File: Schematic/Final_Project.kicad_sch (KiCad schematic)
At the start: 82 parts, among them Q1 PMOS, U1 74HC595, U10 74HC595, U11 74HC595, U12 74HC595, U13 TLC59211IPWR, U14 TLC59211IPWR, U15 TLC59211IPWR, U16 TLC59211IPWR, U17 74HC595, U2 TLC59211IPWR, U3 74HC595, U4 TLC59211IPWR, U5 74HC595, U6 74HC595, U7 TLC59211IPWR, U8 TLC59211IPWR, U9 74HC595

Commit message: SemiFinal Schematic
unknown rgb layout for the Ebay LEDs
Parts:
- removed D1, D10, D11, D12, D13, D14, D15, D16, D17, D18, D19, D2, D20, D21, D22, D23, D24, D25, D26, D27, D28, D29, D3, D30, D31, D32, D33, D34, D35, D36, D37, D38, D39, D4, D40, D41, D42, D43, D44, D45, D46, D47, D48, D49, D5, D50, D51, D52, D53, D54, D55, D56, D57, D58, D59, D6, D60, D61, D62, D63, D64, D7, D8, D9: LED, symbol Device:LED
- removed U1, U10, U11, U12, U3, U5, U6, U9: 74HC595, symbol 74xx:74HC595
- removed U13, U14, U15, U16, U2, U4, U7, U8: TLC59211IPWR, PW20, symbol TLC59211:TLC59211IPWR
- added D1, D10, D11, D12, D13, D14, D15, D16, D17, D18, D19, D2, D20, D21, D22, D23, D24, D25, D26, D27, D28, D29, D3, D30, D31, D32, D33, D34, D35, D36, D37, D38, D39, D4, D40, D41, D42, D43, D44, D45, D46, D47, D48, D49, D5, D50, D51, D52, D53, D54, D55, D56, D57, D58, D59, D6, D60, D61, D62, D63, D64, D7, D8, D9: LED_ARBG, symbol Device:LED_ARBG
- added R_b1, R_b10, R_b11, R_b12, R_b13, R_b14, R_b15, R_b16, R_b17, R_b18, R_b19, R_b2, R_b20, R_b21, R_b22, R_b23, R_b3, R_b4, R_b5, R_b6, R_b65, R_b7, R_b8, R_b9: 1k, symbol Device:R_US
- added U1, U10, U11, U12, U13, U14, U15, U16, U18, U19, U2, U20, U21, U22, U23, U24, U3, U4, U5, U50, U6, U7, U8, U9: TLC5916, symbol Driver_LED:TLC5916
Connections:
- net +5V: now also U1.16 (VDD), U10.16 (VDD), U11.16 (VDD), U12.16 (VDD), U13.16 (VDD), U14.16 (VDD), U15.16 (VDD), U16.16 (VDD), U18.16 (VDD), U19.16 (VDD), U2.16 (VDD), U20.16 (VDD), U21.16 (VDD), U22.16 (VDD), U23.16 (VDD), U24.16 (VDD), U3.16 (VDD), U4.16 (VDD), U5.16 (VDD), U50.16 (VDD), U6.16 (VDD), U7.16 (VDD), U8.16 (VDD), U9.16 (VDD)
- net GND: now also R_b1.1, R_b10.1, R_b11.1, R_b12.1, R_b13.1, R_b14.1, R_b15.1, R_b16.1, R_b17.1, R_b18.1, R_b19.1, R_b2.1, R_b20.1, R_b21.1, R_b22.1, R_b23.1, R_b3.1, R_b4.1, R_b5.1, R_b6.1, R_b65.1, R_b7.1, R_b8.1, R_b9.1, U1.1 (GND), U1.13 (~{OE}(ED2)), U10.1 (GND), U10.13 (~{OE}(ED2)), U11.1 (GND), U11.13 (~{OE}(ED2)), U12.1 (GND), U12.13 (~{OE}(ED2)), U13.1 (GND), U13.13 (~{OE}(ED2)), U14.1 (GND), U14.13 (~{OE}(ED2)), U15.1 (GND), U15.13 (~{OE}(ED2)), U16.1 (GND), U16.13 (~{OE}(ED2)), U18.1 (GND), U18.13 (~{OE}(ED2)), U19.1 (GND), U19.13 (~{OE}(ED2)), U2.1 (GND), U2.13 (~{OE}(ED2)), U20.1 (GND), U20.13 (~{OE}(ED2)), U21.1 (GND), U21.13 (~{OE}(ED2)), U22.1 (GND), U22.13 (~{OE}(ED2)), U23.1 (GND), U23.13 (~{OE}(ED2)), U24.1 (GND), U24.13 (~{OE}(ED2)), U3.1 (GND), U3.13 (~{OE}(ED2)), U4.1 (GND), U4.13 (~{OE}(ED2)), U5.1 (GND), U5.13 (~{OE}(ED2)), U50.1 (GND), U50.13 (~{OE}(ED2)), U6.1 (GND), U6.13 (~{OE}(ED2)), U7.1 (GND), U7.13 (~{OE}(ED2)), U8.1 (GND), U8.13 (~{OE}(ED2)), U9.1 (GND), U9.13 (~{OE}(ED2))
- net at Q1.3 (S): now also D1.1 (A), D10.1 (A), D11.1 (A), D12.1 (A), D13.1 (A), D14.1 (A), D15.1 (A), D16.1 (A), D17.1 (A), D18.1 (A), D19.1 (A), D2.1 (A), D20.1 (A), D21.1 (A), D22.1 (A), D23.1 (A), D24.1 (A), D25.1 (A), D26.1 (A), D27.1 (A), D28.1 (A), D29.1 (A), D3.1 (A), D30.1 (A), D31.1 (A), D32.1 (A), D33.1 (A), D34.1 (A), D35.1 (A), D36.1 (A), D37.1 (A), D38.1 (A), D39.1 (A), D4.1 (A), D40.1 (A), D41.1 (A), D42.1 (A), D43.1 (A), D44.1 (A), D45.1 (A), D46.1 (A), D47.1 (A), D48.1 (A), D49.1 (A), D5.1 (A), D50.1 (A), D51.1 (A), D52.1 (A), D53.1 (A), D54.1 (A), D55.1 (A), D56.1 (A), D57.1 (A), D58.1 (A), D59.1 (A), D6.1 (A), D60.1 (A), D61.1 (A), D62.1 (A), D63.1 (A), D64.1 (A), D7.1 (A), D8.1 (A), D9.1 (A)
- new net: D54.2 (RK), U20.12 (~{OUT7})
- new net: U20.14 (SDO), U21.2 (SDI)
- new net: R_b19.2, U20.15 (R-EXT)
- new net: U19.14 (SDO), U20.2 (SDI)
- new net: D51.3 (BK), U20.5 (~{OUT0})
- new net: D52.2 (RK), U20.6 (~{OUT1})
- new net: D52.4 (GK), U20.7 (~{OUT2})
- new net: D52.3 (BK), U20.8 (~{OUT3})
- new net: D58.3 (BK), U22.10 (~{OUT5})
- new net: D59.2 (RK), U22.11 (~{OUT6})
- new net: D59.4 (GK), U22.12 (~{OUT7})
- new net: U22.14 (SDO), U23.2 (SDI)
- new net: R_b21.2, U22.15 (R-EXT)
- new net: U21.14 (SDO), U22.2 (SDI)
- new net: D57.2 (RK), U22.5 (~{OUT0})
- new net: D57.4 (GK), U22.6 (~{OUT1})
- new net: D57.3 (BK), U22.7 (~{OUT2})
- new net: D58.2 (RK), U22.8 (~{OUT3})
- new net: D58.4 (GK), U22.9 (~{OUT4})
- new net: D49.2 (RK), U19.5 (~{OUT0})
- new net: D49.3 (BK), U19.7 (~{OUT2})
- new net: D49.4 (GK), U19.6 (~{OUT1})
- new net: D14.2 (RK), U4.12 (~{OUT7})
- new net: D14.3 (BK), U5.6 (~{OUT1})
- new net: D14.4 (GK), U5.5 (~{OUT0})
- new net: D32.2 (RK), U11.10 (~{OUT5})
- new net: D32.3 (BK), U11.12 (~{OUT7})
- new net: D32.4 (GK), U11.11 (~{OUT6})
- new net: D24.2 (RK), U8.10 (~{OUT5})
- new net: D24.4 (GK), U8.11 (~{OUT6})
- new net: D24.3 (BK), U8.12 (~{OUT7})
- new net: U8.14 (SDO), U9.2 (SDI)
- new net: R_b8.2, U8.15 (R-EXT)
- new net: U7.14 (SDO), U8.2 (SDI)
- new net: D22.4 (GK), U8.5 (~{OUT0})
- new net: D22.3 (BK), U8.6 (~{OUT1})
- new net: D23.2 (RK), U8.7 (~{OUT2})
- new net: D23.4 (GK), U8.8 (~{OUT3})
- new net: D23.3 (BK), U8.9 (~{OUT4})
- new net: D27.2 (RK), U9.11 (~{OUT6})
- new net: D27.3 (BK), U10.5 (~{OUT0})
- new net: D27.4 (GK), U9.12 (~{OUT7})
- new net: R_b22.2, U23.15 (R-EXT)
- new net: D8.2 (RK), U2.10 (~{OUT5})
- new net: D8.3 (BK), U2.12 (~{OUT7})
- new net: D8.4 (GK), U2.11 (~{OUT6})
- new net: D40.2 (RK), U14.10 (~{OUT5})
- new net: D40.4 (GK), U14.11 (~{OUT6})
- new net: D40.3 (BK), U14.12 (~{OUT7})
- new net: U14.14 (SDO), U15.2 (SDI)
- new net: R_b14.2, U14.15 (R-EXT)
- new net: U13.14 (SDO), U14.2 (SDI)
- new net: D38.4 (GK), U14.5 (~{OUT0})
- new net: D38.3 (BK), U14.6 (~{OUT1})
- new net: D39.2 (RK), U14.7 (~{OUT2})
- new net: D39.4 (GK), U14.8 (~{OUT3})
- new net: D39.3 (BK), U14.9 (~{OUT4})
- new net: D25.2 (RK), U9.5 (~{OUT0})
- new net: D25.3 (BK), U9.7 (~{OUT2})
- new net: D25.4 (GK), U9.6 (~{OUT1})
- new net: D28.2 (RK), U10.6 (~{OUT1})
- new net: D28.3 (BK), U10.8 (~{OUT3})
- new net: D28.4 (GK), U10.7 (~{OUT2})
- new net: D10.2 (RK), U3.8 (~{OUT3})
- new net: D10.3 (BK), U3.10 (~{OUT5})
- new net: D10.4 (GK), U3.9 (~{OUT4})
- new net: U2.14 (SDO), U3.2 (SDI)
- new net: R_b2.2, U2.15 (R-EXT)
- new net: U1.14 (SDO), U2.2 (SDI)
- new net: D6.4 (GK), U2.5 (~{OUT0})
- new net: D6.3 (BK), U2.6 (~{OUT1})
- new net: D7.2 (RK), U2.7 (~{OUT2})
- new net: D7.4 (GK), U2.8 (~{OUT3})
- new net: D7.3 (BK), U2.9 (~{OUT4})
- new net: R_b20.2, U21.15 (R-EXT)
- new net: R_b10.2, U10.15 (R-EXT)
- new net: D60.2 (RK), U23.6 (~{OUT1})
- new net: D60.3 (BK), U23.8 (~{OUT3})
- new net: D60.4 (GK), U23.7 (~{OUT2})
- new net: R_b18.2, U19.15 (R-EXT)
- new net: D54.3 (BK), U21.6 (~{OUT1})
- new net: D54.4 (GK), U21.5 (~{OUT0})
- new net: D36.2 (RK), U13.6 (~{OUT1})
- new net: D36.3 (BK), U13.8 (~{OUT3})
- new net: D36.4 (GK), U13.7 (~{OUT2})
- new net: D50.2 (RK), U19.8 (~{OUT3})
- new net: D50.3 (BK), U19.10 (~{OUT5})
- new net: D50.4 (GK), U19.9 (~{OUT4})
- new net: D17.2 (RK), U6.5 (~{OUT0})
- new net: D17.3 (BK), U6.7 (~{OUT2})
- new net: D17.4 (GK), U6.6 (~{OUT1})
- new net: D55.2 (RK), U21.7 (~{OUT2})
- new net: D55.3 (BK), U21.9 (~{OUT4})
- new net: D55.4 (GK), U21.8 (~{OUT3})
- new net: D6.2 (RK), U1.12 (~{OUT7})
- new net: D4.2 (RK), U1.6 (~{OUT1})
- new net: D4.3 (BK), U1.8 (~{OUT3})
- new net: D4.4 (GK), U1.7 (~{OUT2})
- new net: D59.3 (BK), U23.5 (~{OUT0})
- new net: R_b11.2, U11.15 (R-EXT)
- new net: D62.2 (RK), U23.12 (~{OUT7})
- new net: D62.3 (BK), U24.6 (~{OUT1})
- new net: D62.4 (GK), U24.5 (~{OUT0})
- new net: D48.2 (RK), U18.10 (~{OUT5})
- new net: D48.4 (GK), U18.11 (~{OUT6})
- new net: D48.3 (BK), U18.12 (~{OUT7})
- new net: U18.14 (SDO), U19.2 (SDI)
- new net: R_b17.2, U18.15 (R-EXT)
- new net: U16.14 (SDO), U18.2 (SDI)
- new net: D46.4 (GK), U18.5 (~{OUT0})
- new net: D46.3 (BK), U18.6 (~{OUT1})
- new net: D47.2 (RK), U18.7 (~{OUT2})
- new net: D47.4 (GK), U18.8 (~{OUT3})
- new net: D47.3 (BK), U18.9 (~{OUT4})
- new net: D34.3 (BK), U12.10 (~{OUT5})
- new net: D35.2 (RK), U12.11 (~{OUT6})
- new net: D35.4 (GK), U12.12 (~{OUT7})
- new net: U12.14 (SDO), U13.2 (SDI)
- new net: R_b12.2, U12.15 (R-EXT)
- new net: U11.14 (SDO), U12.2 (SDI)
- new net: D33.2 (RK), U12.5 (~{OUT0})
- new net: D33.4 (GK), U12.6 (~{OUT1})
- new net: D33.3 (BK), U12.7 (~{OUT2})
- new net: D34.2 (RK), U12.8 (~{OUT3})
- new net: D34.4 (GK), U12.9 (~{OUT4})
- new net: D30.2 (RK), U10.12 (~{OUT7})
- new net: U10.14 (SDO), U11.2 (SDI)
- new net: U10.2 (SDI), U9.14 (SDO)
- new net: D22.2 (RK), U7.12 (~{OUT7})
- new net: R_b7.2, U7.15 (R-EXT)
- new net: U6.14 (SDO), U7.2 (SDI)
- new net: D19.3 (BK), U7.5 (~{OUT0})
- new net: D20.2 (RK), U7.6 (~{OUT1})
- new net: D20.4 (GK), U7.7 (~{OUT2})
- new net: D20.3 (BK), U7.8 (~{OUT3})
- new net: D46.2 (RK), U16.12 (~{OUT7})
- new net: R_b16.2, U16.15 (R-EXT)
- new net: U15.14 (SDO), U16.2 (SDI)
- new net: D43.3 (BK), U16.5 (~{OUT0})
- new net: D44.2 (RK), U16.6 (~{OUT1})
- new net: D44.4 (GK), U16.7 (~{OUT2})
- new net: D44.3 (BK), U16.8 (~{OUT3})
- new net: D51.2 (RK), U19.11 (~{OUT6})
- new net: D51.4 (GK), U19.12 (~{OUT7})
- new net: D42.2 (RK), U15.8 (~{OUT3})
- new net: D42.3 (BK), U15.10 (~{OUT5})
- new net: D42.4 (GK), U15.9 (~{OUT4})
- new net: D11.2 (RK), U3.11 (~{OUT6})
- new net: D11.3 (BK), U4.5 (~{OUT0})
- new net: D11.4 (GK), U3.12 (~{OUT7})
- new net: D56.2 (RK), U21.10 (~{OUT5})
- new net: D56.4 (GK), U21.11 (~{OUT6})
- new net: D56.3 (BK), U21.12 (~{OUT7})
- new net: D43.2 (RK), U15.11 (~{OUT6})
- new net: D43.4 (GK), U15.12 (~{OUT7})
- new net: R_b15.2, U15.15 (R-EXT)
- new net: D41.2 (RK), U15.5 (~{OUT0})
- new net: D41.4 (GK), U15.6 (~{OUT1})
- new net: D41.3 (BK), U15.7 (~{OUT2})
- new net: D18.3 (BK), U6.10 (~{OUT5})
- new net: D19.2 (RK), U6.11 (~{OUT6})
- new net: D19.4 (GK), U6.12 (~{OUT7})
- new net: R_b6.2, U6.15 (R-EXT)
- new net: U5.14 (SDO), U6.2 (SDI)
- new net: D18.2 (RK), U6.8 (~{OUT3})
- new net: D18.4 (GK), U6.9 (~{OUT4})
- new net: R_b9.2, U9.15 (R-EXT)
- new net: D12.2 (RK), U4.6 (~{OUT1})
- new net: D12.3 (BK), U4.8 (~{OUT3})
- new net: D12.4 (GK), U4.7 (~{OUT2})
- new net: U4.14 (SDO), U5.2 (SDI)
- new net: R_b4.2, U4.15 (R-EXT)
- new net: U3.14 (SDO), U4.2 (SDI)
- new net: R_b65.2, U1.15 (R-EXT)
- new net: U1.2 (SDI), U50.14 (SDO)
- new net: D3.3 (BK), U1.5 (~{OUT0})
- new net: D38.2 (RK), U13.12 (~{OUT7})
- new net: R_b13.2, U13.15 (R-EXT)
- new net: D9.2 (RK), U3.5 (~{OUT0})
- new net: D9.3 (BK), U3.7 (~{OUT2})
- new net: D9.4 (GK), U3.6 (~{OUT1})
- new net: D31.2 (RK), U11.7 (~{OUT2})
- new net: D31.3 (BK), U11.9 (~{OUT4})
- new net: D31.4 (GK), U11.8 (~{OUT3})
- new net: U23.14 (SDO), U24.2 (SDI)
- new net: D16.2 (RK), U5.10 (~{OUT5})
- new net: D16.3 (BK), U5.12 (~{OUT7})
- new net: D16.4 (GK), U5.11 (~{OUT6})
- new net: D2.2 (RK), U50.8 (~{OUT3})
- new net: D2.3 (BK), U50.10 (~{OUT5})
- new net: D2.4 (GK), U50.9 (~{OUT4})
- new net: D26.3 (BK), U9.10 (~{OUT5})
- new net: D26.2 (RK), U9.8 (~{OUT3})
- new net: D26.4 (GK), U9.9 (~{OUT4})
- new net: D30.4 (GK), U11.5 (~{OUT0})
- new net: D30.3 (BK), U11.6 (~{OUT1})
- new net: D3.2 (RK), U50.11 (~{OUT6})
- new net: D3.4 (GK), U50.12 (~{OUT7})
- new net: R_b1.2, U50.15 (R-EXT)
- new net: D1.2 (RK), U50.5 (~{OUT0})
- new net: D1.4 (GK), U50.6 (~{OUT1})
- new net: D1.3 (BK), U50.7 (~{OUT2})
- new net: D35.3 (BK), U13.5 (~{OUT0})
- new net: R_b3.2, U3.15 (R-EXT)
- new net: R_b5.2, U5.15 (R-EXT)
- new net: D15.2 (RK), U5.7 (~{OUT2})
- new net: D15.4 (GK), U5.8 (~{OUT3})
- new net: D15.3 (BK), U5.9 (~{OUT4})
- new net: D64.2 (RK), U24.10 (~{OUT5})
- new net: D64.4 (GK), U24.11 (~{OUT6})
- new net: D64.3 (BK), U24.12 (~{OUT7})
- new net: R_b23.2, U24.15 (R-EXT)
- new net: D63.2 (RK), U24.7 (~{OUT2})
- new net: D63.4 (GK), U24.8 (~{OUT3})
- new net: D63.3 (BK), U24.9 (~{OUT4})
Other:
- note added: "*Green and Blue on the RGB LEDS are switched compared to the diagram."
- note added: "*No resistors needed for LEDs because current sink limits current."
- note added: "ARGB represents the correct LED layout of the diode."
- company: (none) -> ZesTM32
- title: 8^3 LED Cube Layer Expandable Schematic -> 8^3 RGB LED Cube Layer Expandable Schematic
- moved on the sheet: Q1, U17

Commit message: Fixed open wires, semifinalfinal schematic
i hate myself
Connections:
- net at U20.10 (~{OUT5}): now also D53.4 (GK)
- net at U20.11 (~{OUT6}): now also D53.3 (BK)
- net at U20.9 (~{OUT4}): now also D53.2 (RK)
- net at D13.2 (RK): now also U4.9 (~{OUT4})
- net at D13.3 (BK): now also U4.11 (~{OUT6})
- net at D13.4 (GK): now also U4.10 (~{OUT5})
- net at D21.2 (RK): now also U7.9 (~{OUT4})
- net at D21.3 (BK): now also U7.11 (~{OUT6})
- net at D21.4 (GK): now also U7.10 (~{OUT5})
- net at D37.2 (RK): now also U13.9 (~{OUT4})
- net at D37.3 (BK): now also U13.11 (~{OUT6})
- net at D37.4 (GK): now also U13.10 (~{OUT5})
- net at U10.10 (~{OUT5}): now also D29.4 (GK)
- net at U10.11 (~{OUT6}): now also D29.3 (BK)
- net at U10.9 (~{OUT4}): now also D29.2 (RK)
- net at U16.10 (~{OUT5}): now also D45.4 (GK)
- net at U16.11 (~{OUT6}): now also D45.3 (BK)
- net at U16.9 (~{OUT4}): now also D45.2 (RK)
- net at U1.10 (~{OUT5}): now also D5.4 (GK)
- net at U1.11 (~{OUT6}): now also D5.3 (BK)
- net at U1.9 (~{OUT4}): now also D5.2 (RK)
- net at U23.10 (~{OUT5}): now also D61.4 (GK)
- net at U23.11 (~{OUT6}): now also D61.3 (BK)
- net at U23.9 (~{OUT4}): now also D61.2 (RK)

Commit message: Added Comparator Setup
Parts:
- added R_b24: 33k, symbol Device:R_US
- added R_b25: 22k, symbol Device:R_US
- added U25: LM393, symbol Comparator:LM393
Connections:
- net +5V: now also R_b24.2, U25.8 (V+)
- net GND: now also R_b25.1, U25.4 (V-)
- new net: R_b24.1, R_b25.2, U25.2 (-)
- new net TLC5916: U25.1
- new net V_stm32: U25.3 (+)
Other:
- note added: "Comparator Setup for SI, CLK, and LE(ED1) inputs:"
- note added: "Layer of LED Matrix Setup"
- moved on the sheet: D1, D10, D11, D12, D13, D14, D15, D16, D17, D18, D19, D2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

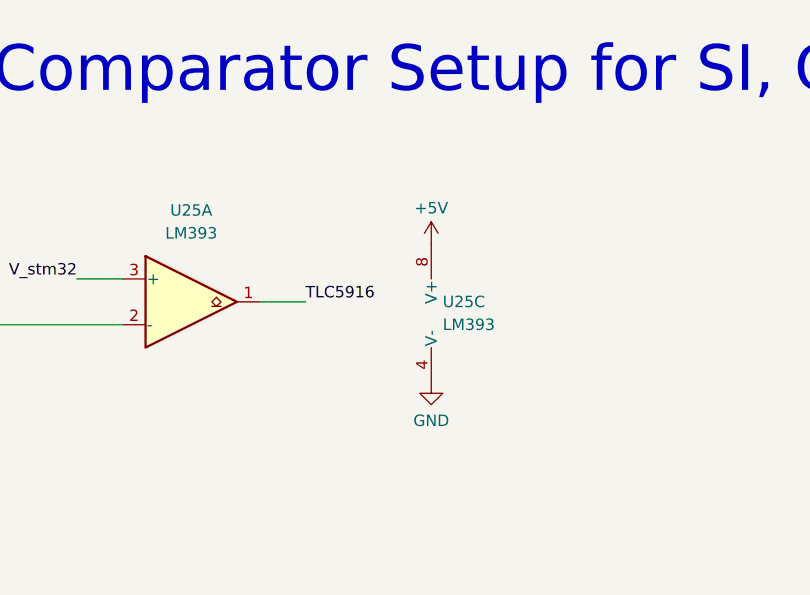
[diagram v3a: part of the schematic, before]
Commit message: Added Pullup resistor to comparator setup
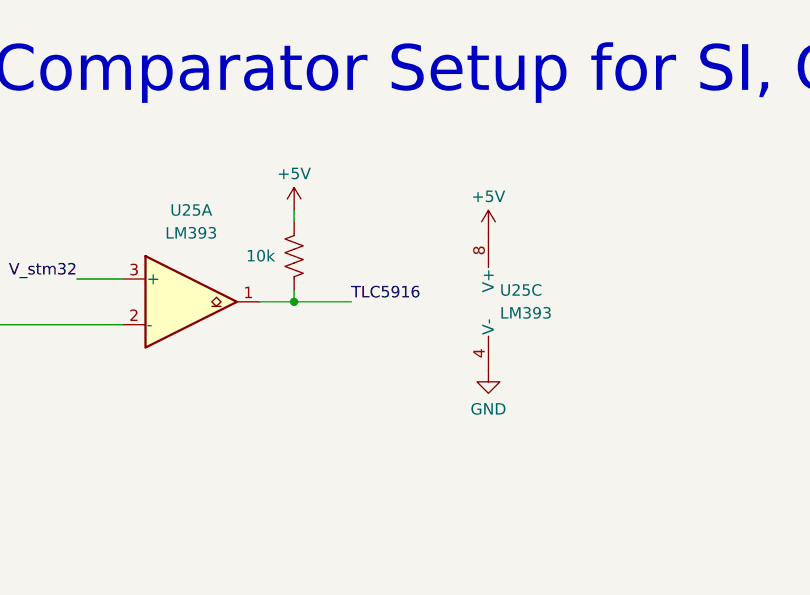
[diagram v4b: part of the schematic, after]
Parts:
- added R_b26: 10k, symbol Device:R_US
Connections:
- net +5V: now also R_b26.2
- net TLC5916: now also R_b26.1
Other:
- moved on the sheet: U25C
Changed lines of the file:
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@@
 	)
 	(junction
+		(at 1424.94 81.28)
+		(diameter 0)
+		(color 0 0 0 0)
+	)
+	(junction
 		(at 1083.31 248.92)
 		(diameter 0)
@@
 	(wire
 		(pts
+			(xy 1424.94 71.12) (xy 1424.94 72.39)
+		)
+		(stroke
+			(width 0)
+			(type default)
+		)
+	)
+	(wire
+		(pts
 			(xy 450.85 273.05) (xy 502.92 273.05)
 		)
@@
 	(wire
 		(pts
+			(xy 1424.94 81.28) (xy 1431.29 81.28)
+		)
+		(stroke
+			(width 0)
+			(type default)
+		)
+	)
+	(wire
+		(pts
 			(xy 589.28 337.82) (xy 595.63 337.82)
 		)
@@
 	(wire
 		(pts
-			(xy 1421.13 81.28) (xy 1426.21 81.28)
+			(xy 1421.13 81.28) (xy 1424.94 81.28)
 		)
 		(stroke
@@
 	(wire
 		(pts
+			(xy 1424.94 80.01) (xy 1424.94 81.28)
+		)
+		(stroke
+			(width 0)
+			(type default)
+		)
+	)
+	(wire
+		(pts
 			(xy 300.99 163.83) (xy 300.99 415.29)
 		)
@@
 	)
 	(label "TLC5916"
-		(at 1426.21 81.28 0)
+		(at 1431.29 81.28 0)
 		(fields_autoplaced yes)
 		(effects
@@
 	)
 	(symbol
+		(lib_id "Device:R_US")
+		(at 1424.94 76.2 0)
+		(mirror x)
+		(unit 1)
+		(exclude_from_sim no)
+		(in_bom yes)
+		(on_board yes)
+		(dnp no)
+		(property "Reference" "R_b26"
+			(at 1426.464 77.216 0)
+			(effects
+				(font
+					(size 1.27 1.27)
+				)
+				(justify left)
+				(hide yes)
+			)
+		)
+		(property "Value" "10k"
+			(at 1419.606 76.2 0)
+			(effects
+				(font
+					(size 1.27 1.27)
+				)
+				(justify left)
+			)
+		)
+		(property "Footprint" ""
+			(at 1425.956 75.946 90)
+			(effects
+				(font
+					(size 1.27 1.27)
+				)
+				(hide yes)
+			)
+		)
+		(property "Datasheet" "~"
+			(at 1424.94 76.2 0)
+			(effects
+				(font
+					(size 1.27 1.27)
+				)
+				(hide yes)
+			)
+		)
+		(property "Description" "Resistor, US symbol"
+			(at 1424.94 76.2 0)
+			(effects
+				(font
+					(size 1.27 1.27)
+				)
+				(hide yes)
+			)
+		)
+		(pin "2"
+		)
+		(pin "1"
+		)
+		(instances
+			(project "Final_Project"
+				(path "/e655de0a-a1bb-4f4d-bf06-87625b45f4ee"
+					(reference "R_b26")
+					(unit 1)
+				)
+			)
+		)
+	)
+	(symbol
 		(lib_id "power:GND")
 		(at 424.18 533.4 0)
@@
 	(symbol
 		(lib_id "power:GND")
-		(at 1440.18 90.17 0)
+		(at 1446.53 88.9 0)
 		(unit 1)
 		(exclude_from_sim no)
@@
 		(dnp no)
 		(property "Reference" "#PWR0101"
-			(at 1440.18 96.52 0)
+			(at 1446.53 95.25 0)
 			(effects
 				(font
@@
 		)
 		(property "Value" "GND"
-			(at 1440.18 94.488 0)
+			(at 1446.53 93.218 0)
 			(effects
 				(font
@@
 		)
 		(property "Footprint" ""
-			(at 1440.18 90.17 0)
+			(at 1446.53 88.9 0)
 			(effects
 				(font
@@
 		)
 		(property "Datasheet" ""
-			(at 1440.18 90.17 0)
+			(at 1446.53 88.9 0)
 			(effects
 				(font
@@
 		)
 		(property "Description" "Power symbol creates a global label with name \"GND\" , ground"
-			(at 1440.18 90.17 0)
+			(at 1446.53 88.9 0)
 			(effects
 				(font
@@
 	)
 	(symbol
+		(lib_id "power:+5V")
+		(at 1424.94 71.12 0)
+		(unit 1)
+		(exclude_from_sim no)
+		(in_bom yes)
+		(on_board yes)
+		(dnp no)
+		(property "Reference" "#PWR0104"
+			(at 1424.94 74.93 0)
+			(effects
+				(font
+					(size 1.27 1.27)
+				)
+				(hide yes)
+			)
+		)
+		(property "Value" "+5V"
+			(at 1424.94 67.056 0)
+			(effects
+				(font
+					(size 1.27 1.27)
+				)
+			)
+		)
+		(property "Footprint" ""
+			(at 1424.94 71.12 0)
+			(effects
+				(font
+					(size 1.27 1.27)
+				)
+				(hide yes)
+			)
+		)
+		(property "Datasheet" ""
+			(at 1424.94 71.12 0)
+			(effects
+				(font
+					(size 1.27 1.27)
+				)
+				(hide yes)
+			)
+		)
+		(property "Description" "Power symbol creates a global label with name \"+5V\""
+			(at 1424.94 71.12 0)
+			(effects
+				(font
+					(size 1.27 1.27)
+				)
+				(hide yes)
+			)
+		)
+		(pin "1"
+		)
+		(instances
+			(project "Final_Project"
+				(path "/e655de0a-a1bb-4f4d-bf06-87625b45f4ee"
+					(reference "#PWR0104")
+					(unit 1)
+				)
+			)
+		)
+	)
+	(symbol
 		(lib_id "Device:LED_ARBG")
 		(at 1261.11 307.34 0)
@@
 	(symbol
 		(lib_id "power:+5V")
-		(at 1440.18 74.93 0)
+		(at 1446.53 73.66 0)
 		(unit 1)
 		(exclude_from_sim no)
@@
 		(dnp no)
 		(property "Reference" "#PWR099"
-			(at 1440.18 78.74 0)
+			(at 1446.53 77.47 0)
 			(effects
 				(font
@@
 		)
 		(property "Value" "+5V"
-			(at 1440.18 70.866 0)
+			(at 1446.53 69.596 0)
 			(effects
 				(font
@@
 		)
 		(property "Footprint" ""
-			(at 1440.18 74.93 0)
+			(at 1446.53 73.66 0)
 			(effects
 				(font
@@
 		)
 		(property "Datasheet" ""
-			(at 1440.18 74.93 0)
+			(at 1446.53 73.66 0)
 			(effects
 				(font
@@
 		)
 		(property "Description" "Power symbol creates a global label with name \"+5V\""
-			(at 1440.18 74.93 0)
+			(at 1446.53 73.66 0)
 			(effects
 				(font
@@
 	(symbol
 		(lib_id "Comparator:LM393")
-		(at 1442.72 82.55 0)
+		(at 1449.07 81.28 0)
 		(unit 3)
 		(exclude_from_sim no)
@@
 		(fields_autoplaced yes)
 		(property "Reference" "U25"
-			(at 1441.45 81.2799 0)
+			(at 1447.8 80.0099 0)
 			(effects
 				(font
@@
 		)
 		(property "Value" "LM393"
-			(at 1441.45 83.8199 0)
+			(at 1447.8 82.5499 0)
 			(effects
 				(font
@@
 		)
 		(property "Footprint" ""
-			(at 1442.72 82.55 0)
+			(at 1449.07 81.28 0)
 			(effects
 				(font
@@
 		)
 		(property "Datasheet" "http://www.ti.com/lit/ds/symlink/lm393.pdf"
-			(at 1442.72 82.55 0)
+			(at 1449.07 81.28 0)
 			(effects
 				(font
@@
 		)
 		(property "Description" "Low-Power, Low-Offset Voltage, Dual Comparators, DIP-8/SOIC-8/TO-99-8"
-			(at 1442.72 82.55 0)
+			(at 1449.07 81.28 0)
 			(effects
 				(font
